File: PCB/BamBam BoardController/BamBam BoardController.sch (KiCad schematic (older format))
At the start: 32 parts, among them U1 TEENSY_3.1+4, U2 HC_05, U5 LC78_03-1.0, X1 Supply

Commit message: Auf BamBam angepasst. HC-05 Rahmen lag auf Pads BrmesOpto Text durch Bremse erstezt Gerber und Drill-Dateien generiert und gesichtet
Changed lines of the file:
@@
 LIBS:contrib
 LIBS:valves
-LIBS:Teensy-cache
+LIBS:BamBam BoardController-cache
 EELAYER 25 0
 EELAYER END
@@
 encoding utf-8
 Sheet 1 2
-Title "Elektroskate Teensy"
+Title "BamBam BoardController"
 Date "19.02.2015"
 Rev "1.0"
@@
 S 7100 6200 500  150
 U 54E61B75
-F0 "TeensyS2" 60
-F1 "TeensyS2.sch" 60
+F0 "BamBam BoardController" 60
+F1 "BamBam BoardControllerS2.sch" 60
 $EndSheet
 Text Label 6250 1250 0    60   ~ 0

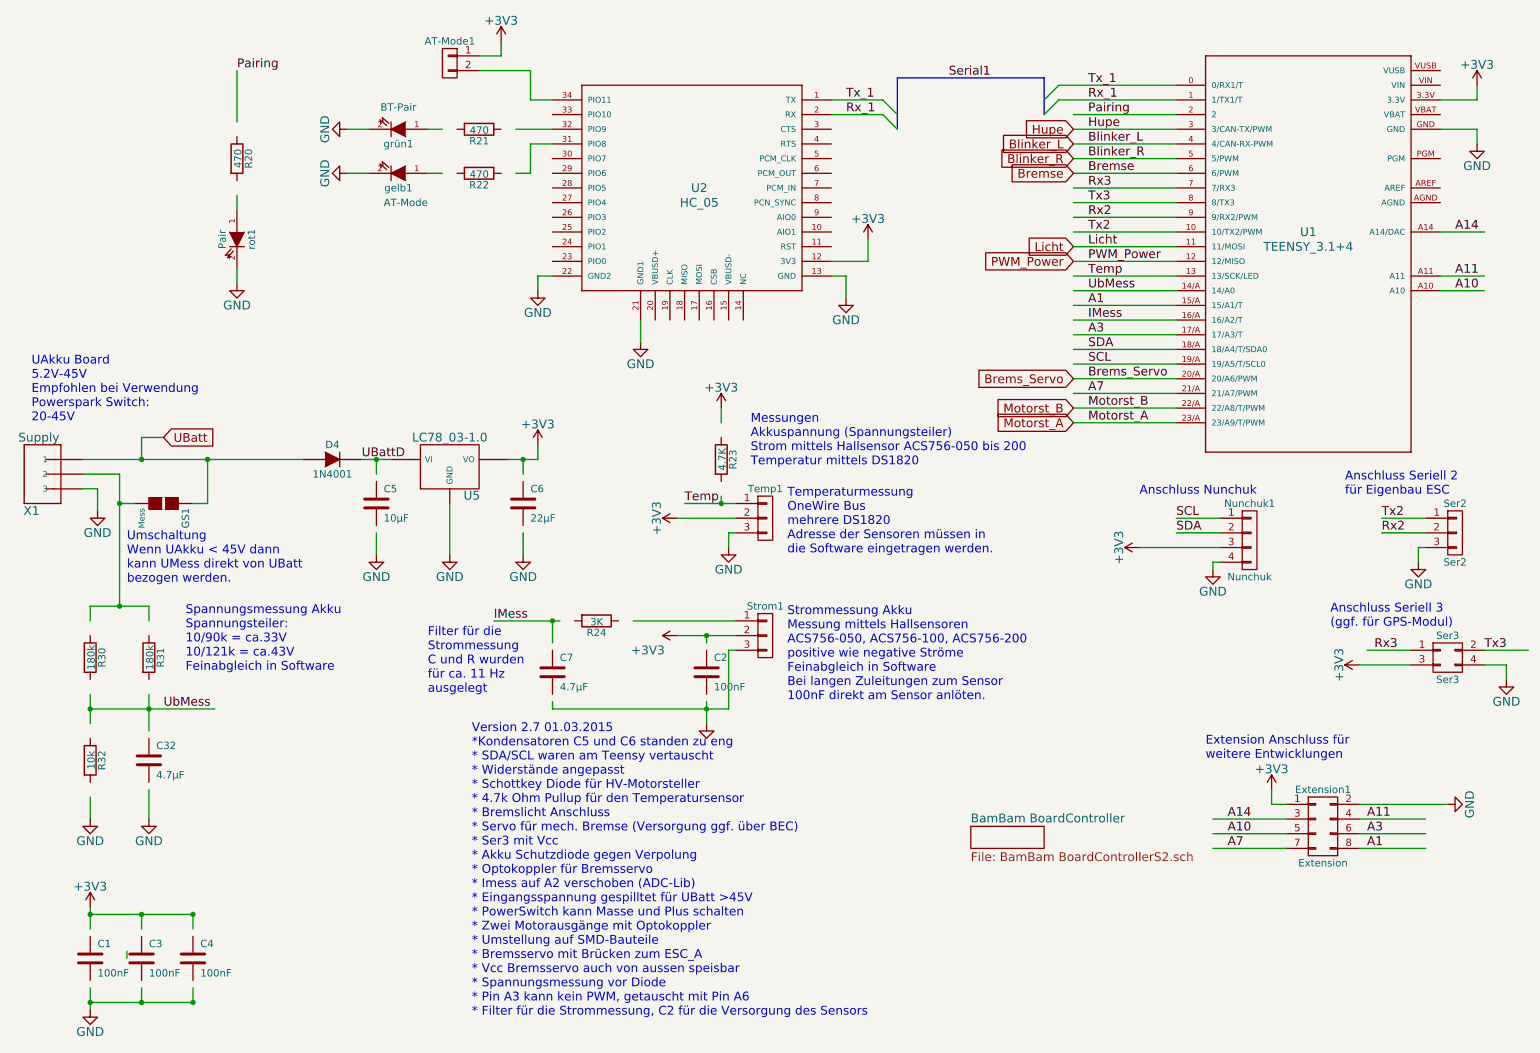
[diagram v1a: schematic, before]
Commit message: Anpassung an die KiCAD Libs >02/2015 Einige kleine Korrekturen am Layout Anpassung der Mounting Holes mit NTPH (nicht durch kontaktieren) Zwei Texte im PCB zugefügt (Tx und Rx Ser2)
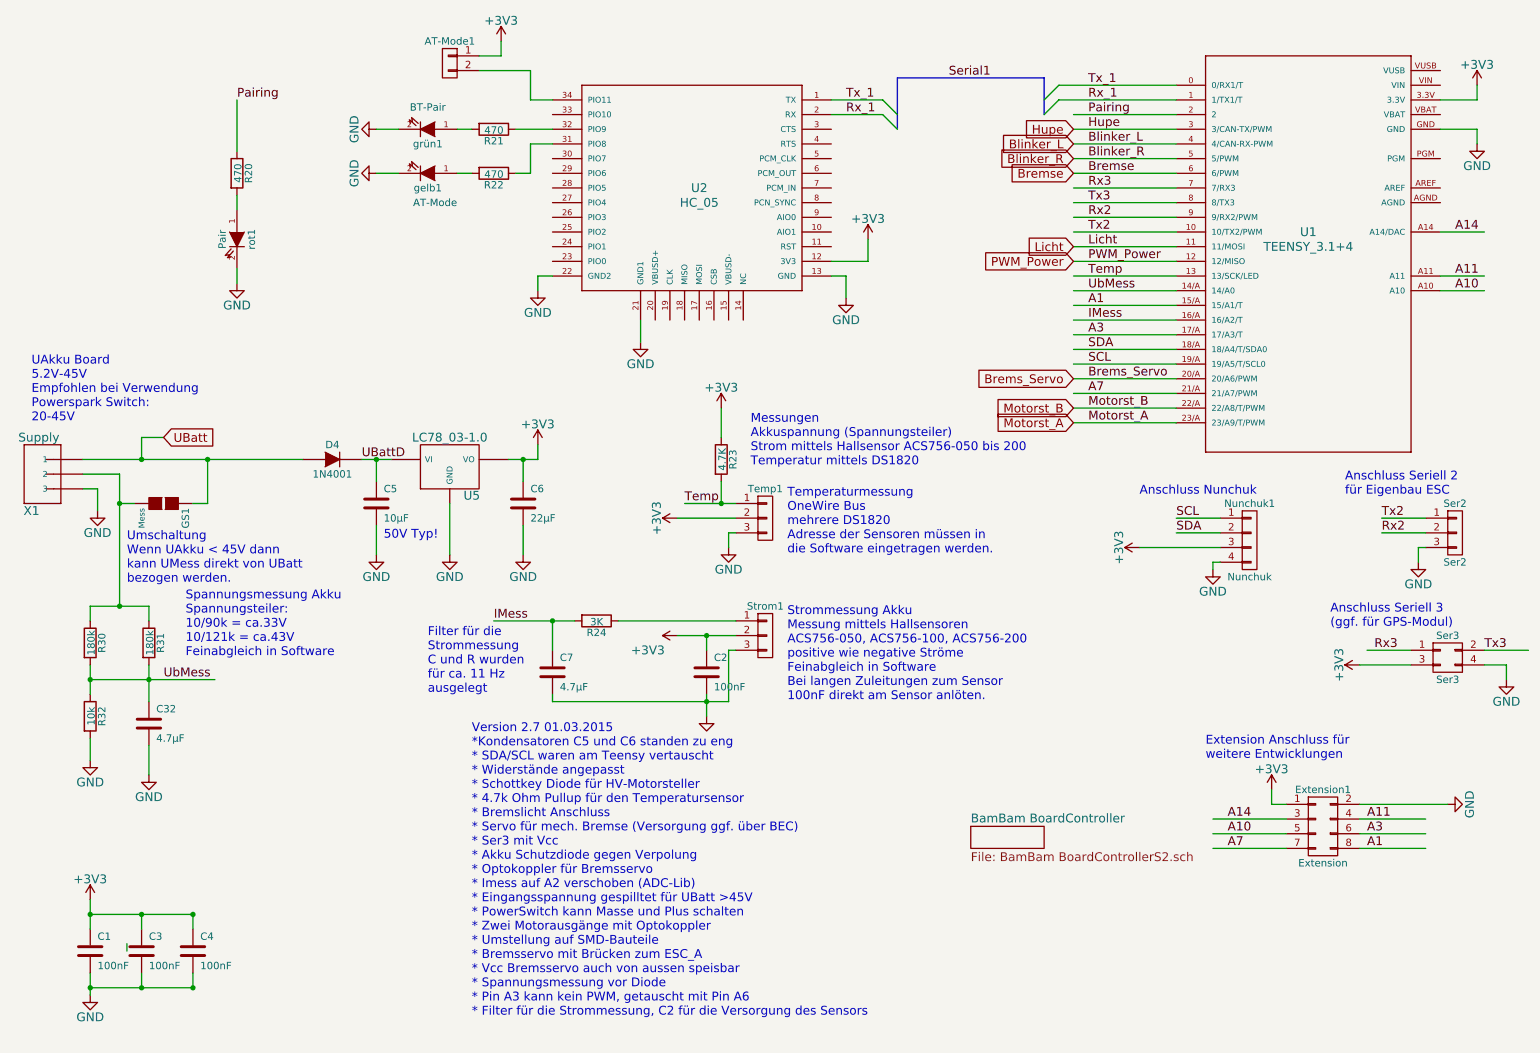
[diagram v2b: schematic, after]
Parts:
- U1: footprint packages:Teensy_3_Series_Board_v1.0-TEENSY_3.1+4 -> Teensy_3_Series_Board_v1.0:Teensy_3_Series_Board_v1.0-TEENSY_3.1+4
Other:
- note added: "50V Typ!"
- moved on the sheet: C1, C3, C32, C4, R20, R21, R22, R30, R31, R32, gelb1, grün1

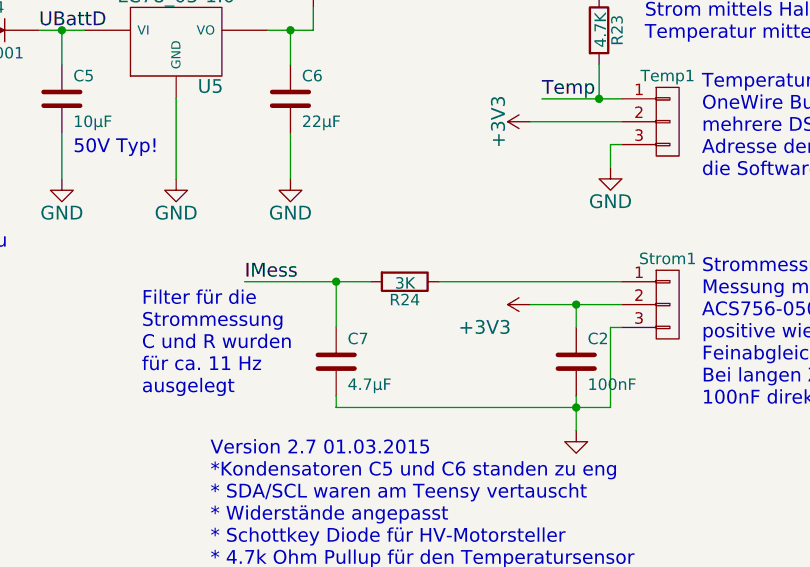
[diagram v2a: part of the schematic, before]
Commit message: Die Version 2.71 hat einige Veränderungen in den Bestückungstext bekommen, Verdeckte Texte wurden Verlagert und noch weitere Informationen an den Anschlüssen ergänzt. Eine Leiterbahn wurde im Querschnitt vergrößert und andere schöner verlegt.
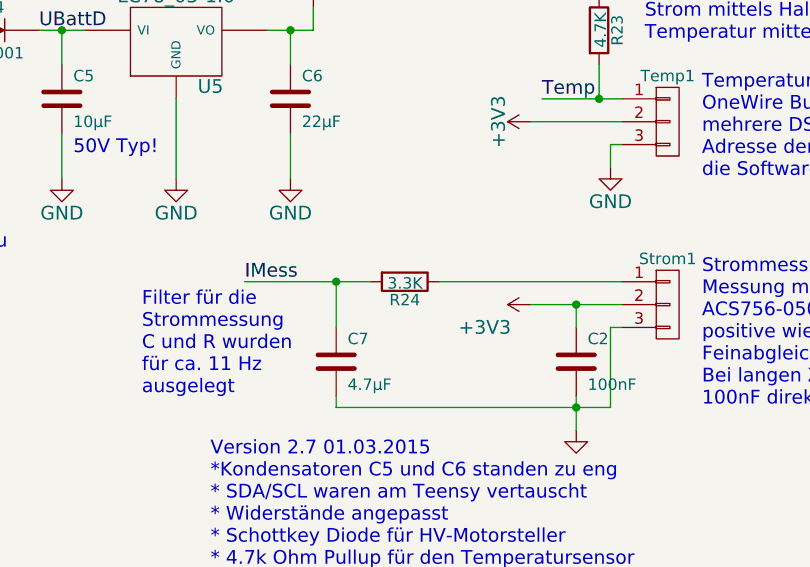
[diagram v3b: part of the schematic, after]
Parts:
- R24: value 3K -> 3.3K
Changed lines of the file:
@@
 P 4550 4800
 F 0 "R24" V 4630 4800 50  0000 C CNN
-F 1 "3K" V 4557 4801 50  0000 C CNN
+F 1 "3.3K" V 4557 4801 50  0000 C CNN
 F 2 "Resistors_SMD:R_1206" V 4480 4800 30  0001 C CNN
 F 3 "" H 4550 4800 30  0000 C CNN
